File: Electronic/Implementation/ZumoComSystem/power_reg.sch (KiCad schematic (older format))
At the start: 5 parts, among them J1 AudioJack2_SwitchT, U1 LT1374CS8-5PBF, U2 TPS62056DGS

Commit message: electronic -> Schematic -> add hierarchical pins, modified Regulator page
           -> BOM & Clac: add new inductors
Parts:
- removed J1: AudioJack2_SwitchT, Button_Switch_THT:SW_E-Switch_EG1224_SPDT_Angled, symbol Connector:AudioJack2_SwitchT
- added C1, C?: >10u, symbol Device:C
- added C2: >22u, symbol Device:C
- added C? (x3): C, symbol Device:C
- added D?: D, symbol Device:D
- added M1: MPMOS, symbol pspice:MPMOS
- added SW1: MLL1200S, SW_MLL1200S, symbol MLL1200S:MLL1200S
- L2: value 6uH -> 22uH
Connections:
- net labels added: +3V3, +5V, GND, V_Bat
- wire segments 2 -> 72
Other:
- moved on the sheet: L1, L2, U1, U2

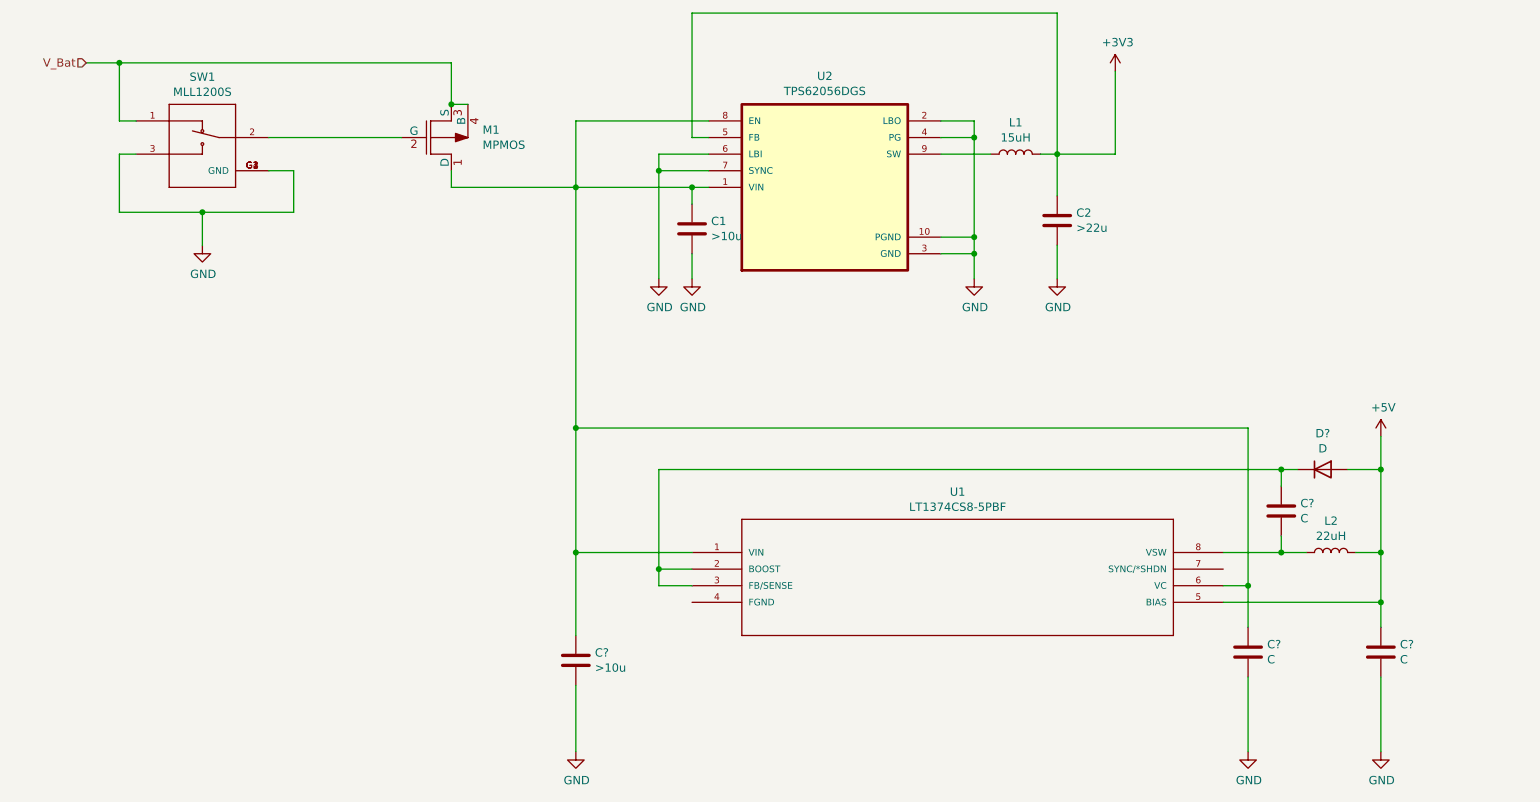
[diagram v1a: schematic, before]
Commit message: Electronic -> Schematic -> DC/DC -> add C, L with footprint, datasheet
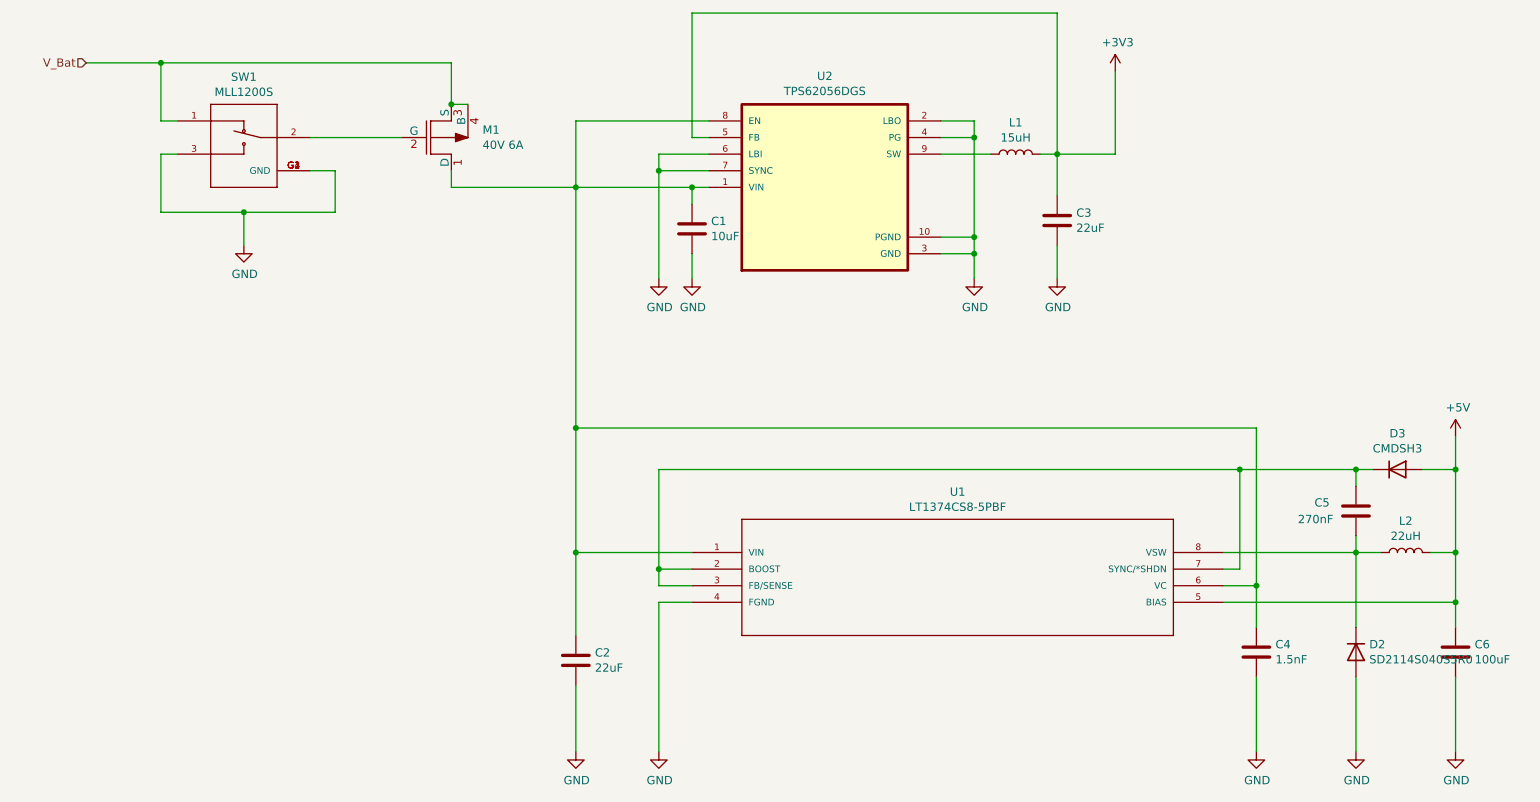
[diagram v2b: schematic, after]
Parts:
- removed C2: >22u, symbol Device:C
- added C3: 22uF, Capacitor_SMD:C_1206_3216Metric_Pad1.42x1.75mm_HandSolder, symbol Device:C
- added D2: SD2114S040S5R0, Diode_SMD:D_2114_3652Metric_Pad1.85x3.75mm_HandSolder, symbol Device:D
- C1: value >10u -> 10uF; footprint (none) -> Capacitor_SMD:C_0805_2012Metric_Pad1.15x1.40mm_HandSolder
- C2: renamed from C?; value >10u -> 22uF; footprint (none) -> Capacitor_SMD:C_1206_3216Metric_Pad1.42x1.75mm_HandSolder
- C4: renamed from C?; value C -> 1.5nF; footprint (none) -> Capacitor_SMD:C_0603_1608Metric_Pad1.05x0.95mm_HandSolder
- C5: renamed from C?; value C -> 270nF; footprint (none) -> Capacitor_SMD:C_0805_2012Metric_Pad1.15x1.40mm_HandSolder
- C6: renamed from C?; value C -> 100uF; footprint (none) -> Capacitor_SMD:C_1206_3216Metric_Pad1.42x1.75mm_HandSolder
- D3: renamed from D?; value D -> CMDSH3; footprint (none) -> Diode_SMD:D_SOD-323
- M1: value MPMOS -> 40V 6A; footprint (none) -> Package_TO_SOT_SMD:SOT-89-3_Handsoldering
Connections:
- net +3V3: now also C3.1
- net GND: now also U1.4 (FGND), C3.2, D2.2 (A)
- net at C5.1, D3.1 (K), U1.2 (BOOST)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: now also U1.7 (SYNC/*SHDN)
- net at C5.2, L2.1, U1.8 (VSW): now also D2.1 (K)
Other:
- moved on the sheet: C4, C5, C6, D3, L2, SW1

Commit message: Electronic: Schematic: ESP I/Os, IF_Pololu Pins, USB_max
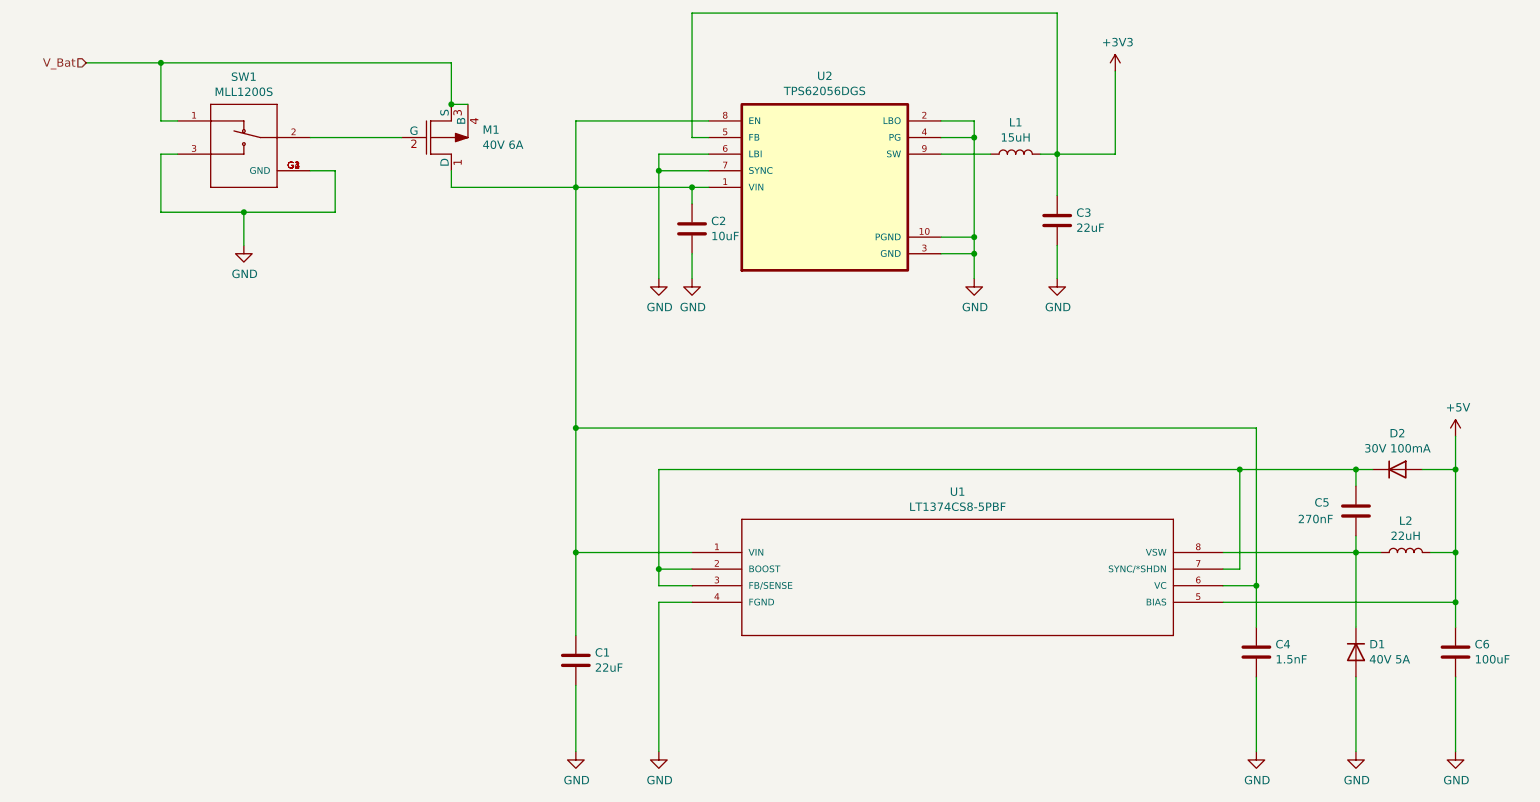
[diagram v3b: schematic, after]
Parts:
- D1: renamed from D2; value SD2114S040S5R0 -> 40V 5A
- D2: renamed from D3; value CMDSH3 -> 30V 100mA
- renumbered C2 to C1, C1 to C2
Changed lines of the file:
@@
 Sheet 2 7
 Title "Zumo Communication System"
-Date "2021-06-25"
+Date "2021-07-28"
 Rev "V1.0"
 Comp "NewTec GmbH"
@@
 V_Bat
 $Comp
-L power:+3V3 #PWR0101
+L power:+3V3 #PWR08
 U 1 1 60CC7A1E
 P 7200 1300
-F 0 "#PWR0101" H 7200 1150 50  0001 C CNN
+F 0 "#PWR08" H 7200 1150 50  0001 C CNN
 F 1 "+3V3" H 7215 1473 50  0000 C CNN
 F 2 "" H 7200 1300 50  0001 C CNN
@@
 $EndComp
 $Comp
-L power:+5V #PWR0102
+L power:+5V #PWR011
 U 1 1 60CC818D
 P 9250 3500
-F 0 "#PWR0102" H 9250 3350 50  0001 C CNN
+F 0 "#PWR011" H 9250 3350 50  0001 C CNN
 F 1 "+5V" H 9265 3673 50  0000 C CNN
 F 2 "" H 9250 3500 50  0001 C CNN
@@
 	4750 1600 3950 1600
 $Comp
-L power:GND #PWR0103
+L power:GND #PWR06
 U 1 1 60CDA80F
 P 6350 2550
-F 0 "#PWR0103" H 6350 2300 50  0001 C CNN
+F 0 "#PWR06" H 6350 2300 50  0001 C CNN
 F 1 "GND" H 6355 2377 50  0000 C CNN
 F 2 "" H 6350 2550 50  0001 C CNN
@@
 Connection ~ 6350 2300
 $Comp
-L power:GND #PWR0104
+L power:GND #PWR03
 U 1 1 60CDABA5
 P 4450 2550
-F 0 "#PWR0104" H 4450 2300 50  0001 C CNN
+F 0 "#PWR03" H 4450 2300 50  0001 C CNN
 F 1 "GND" H 4455 2377 50  0000 C CNN
 F 2 "" H 4450 2550 50  0001 C CNN
@@
 	6850 1800 6750 1800
 $Comp
-L Device:C C1
+L Device:C C2
 U 1 1 60CE065A
 P 4650 2250
-F 0 "C1" H 4765 2296 50  0000 L CNN
+F 0 "C2" H 4765 2296 50  0000 L CNN
 F 1 "10uF" H 4765 2205 50  0000 L CNN
 F 2 "Capacitor_SMD:C_0805_2012Metric_Pad1.15x1.40mm_HandSolder" H 4688 2100 50  0001 C CNN
@@
 	4650 2400 4650 2550
 $Comp
-L power:GND #PWR0105
+L power:GND #PWR05
 U 1 1 60CE2DC8
 P 4650 2550
-F 0 "#PWR0105" H 4650 2300 50  0001 C CNN
+F 0 "#PWR05" H 4650 2300 50  0001 C CNN
 F 1 "GND" H 4655 2377 50  0000 C CNN
 F 2 "" H 4650 2550 50  0001 C CNN
@@
 $EndComp
 $Comp
-L power:GND #PWR0106
+L power:GND #PWR07
 U 1 1 60CE2EFC
 P 6850 2550
-F 0 "#PWR0106" H 6850 2300 50  0001 C CNN
+F 0 "#PWR07" H 6850 2300 50  0001 C CNN
 F 1 "GND" H 6855 2377 50  0000 C CNN
 F 2 "" H 6850 2550 50  0001 C CNN
@@
 	3200 1900 3200 2000
 $Comp
-L power:GND #PWR0107
+L power:GND #PWR01
 U 1 1 60CF3E43
 P 1950 2350
-F 0 "#PWR0107" H 1950 2100 50  0001 C CNN
+F 0 "#PWR01" H 1950 2100 50  0001 C CNN
 F 1 "GND" H 1955 2177 50  0000 C CNN
 F 2 "" H 1950 2350 50  0001 C CNN
@@
 Wire Wire Line
 	1950 2150 2500 2150
-$Comp
-L pspice:MPMOS M1
-U 1 1 60D049A0
-P 3100 1700
-F 0 "M1" H 3388 1746 50  0000 L CNN
-F 1 "40V 6A" H 3388 1655 50  0000 L CNN
-F 2 "Package_TO_SOT_SMD:SOT-89-3_Handsoldering" H 3100 1700 50  0001 C CNN
-F 3 "https://my.centralsemi.com/datasheets/CXDM4060P.PDF" H 3100 1700 50  0001 C CNN
-	1    3100 1700
-	1    0    0    -1
-$EndComp
 Wire Wire Line
 	3300 1500 3200 1500
 Connection ~ 3200 1500
 $Comp
-L Device:C C2
+L Device:C C1
 U 1 1 60D11B75
 P 3950 4850
-F 0 "C2" H 4065 4896 50  0000 L CNN
+F 0 "C1" H 4065 4896 50  0000 L CNN
 F 1 "22uF" H 4065 4805 50  0000 L CNN
 F 2 "Capacitor_SMD:C_1206_3216Metric_Pad1.42x1.75mm_HandSolder" H 3988 4700 50  0001 C CNN
@@
 	4650 4300 4450 4300
 $Comp
-L power:GND #PWR01
+L power:GND #PWR02
 U 1 1 60D140B6
 P 3950 5400
-F 0 "#PWR01" H 3950 5150 50  0001 C CNN
+F 0 "#PWR02" H 3950 5150 50  0001 C CNN
 F 1 "GND" H 3955 5227 50  0000 C CNN
 F 2 "" H 3950 5400 50  0001 C CNN
@@
 	3950 5400 3950 5000
 $Comp
-L Device:D D3
+L Device:D D2
 U 1 1 60D196DD
 P 8900 3700
-F 0 "D3" H 8900 3917 50  0000 C CNN
-F 1 "CMDSH3 " H 8900 3826 50  0000 C CNN
+F 0 "D2" H 8900 3917 50  0000 C CNN
+F 1 "30V 100mA" H 8900 3826 50  0000 C CNN
 F 2 "Diode_SMD:D_SOD-323" H 8900 3700 50  0001 C CNN
 F 3 "https://my.centralsemi.com/datasheets/CMDSH-3.PDF" H 8900 3700 50  0001 C CNN
@@
 	8050 4650 8050 4400
 $Comp
-L power:GND #PWR03
+L power:GND #PWR09
 U 1 1 60D2AA9B
 P 8050 5400
-F 0 "#PWR03" H 8050 5150 50  0001 C CNN
+F 0 "#PWR09" H 8050 5150 50  0001 C CNN
 F 1 "GND" H 8055 5227 50  0000 C CNN
 F 2 "" H 8050 5400 50  0001 C CNN
@@
 $EndComp
 $Comp
-L power:GND #PWR05
+L power:GND #PWR012
 U 1 1 60D2B041
 P 9250 5400
-F 0 "#PWR05" H 9250 5150 50  0001 C CNN
+F 0 "#PWR012" H 9250 5150 50  0001 C CNN
 F 1 "GND" H 9255 5227 50  0000 C CNN
 F 2 "" H 9250 5400 50  0001 C CNN
@@
 	9250 3700 9250 3500
 $Comp
-L Device:D D2
+L Device:D D1
 U 1 1 60D62CCC
 P 8650 4800
-F 0 "D2" V 8604 4880 50  0000 L CNN
-F 1 "SD2114S040S5R0" V 8695 4880 50  0000 L CNN
+F 0 "D1" V 8604 4880 50  0000 L CNN
+F 1 "40V 5A" V 8695 4880 50  0000 L CNN
 F 2 "Diode_SMD:D_2114_3652Metric_Pad1.85x3.75mm_HandSolder" H 8650 4800 50  0001 C CNN
 F 3 "https://datasheets.avx.com/schottky.pdf" H 8650 4800 50  0001 C CNN
@@
 $EndComp
 $Comp
-L power:GND #PWR04
+L power:GND #PWR010
 U 1 1 60D630D3
 P 8650 5400
-F 0 "#PWR04" H 8650 5150 50  0001 C CNN
+F 0 "#PWR010" H 8650 5150 50  0001 C CNN
 F 1 "GND" H 8655 5227 50  0000 C CNN
 F 2 "" H 8650 5400 50  0001 C CNN
@@
 	4450 4500 4450 5400
 $Comp
-L power:GND #PWR02
+L power:GND #PWR04
 U 1 1 60D67CF9
 P 4450 5400
-F 0 "#PWR02" H 4450 5150 50  0001 C CNN
+F 0 "#PWR04" H 4450 5150 50  0001 C CNN
 F 1 "GND" H 4455 5227 50  0000 C CNN
 F 2 "" H 4450 5400 50  0001 C CNN
@@
 Wire Wire Line
 	1000 1250 1450 1250
+$Comp
+L pspice:MPMOS M1
+U 1 1 60D049A0
+P 3100 1700
+F 0 "M1" H 3388 1746 50  0000 L CNN
+F 1 "40V 6A" H 3388 1655 50  0000 L CNN
+F 2 "Package_TO_SOT_SMD:SOT-89-3_Handsoldering" H 3100 1700 50  0001 C CNN
+F 3 "https://my.centralsemi.com/datasheets/CXDM4060P.PDF" H 3100 1700 50  0001 C CNN
+	1    3100 1700
+	1    0    0    -1
+$EndComp
 $EndSCHEMATC

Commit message: Electronic: no charger, added Cp2102 instead of Ft232, first palcement
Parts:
- removed M1: 40V 6A, Package_TO_SOT_SMD:SOT-89-3_Handsoldering, symbol pspice:MPMOS
- added Q1: Q_PMOS_GDS, footprints:TSOT-23-6_HandSoldering, symbol Device:Q_PMOS_GDS
- added R1, R2: 100k, Resistor_SMD:R_0603_1608Metric_Pad1.05x0.95mm_HandSolder, symbol Device:R
- L1: footprint Inductor_SMD:L_Wuerth_HCI-1040 -> footprints:L_Wuerth_HCI-1040_3D
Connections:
- net GND: now also R2.1
- net V_Bat: now also Q1.3 (S)
- net at C1.1, C2.1, C4.1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: now also Q1.2 (D)
- net at SW1.2: now also R1.2
- new net: Q1.1 (G), R1.1, R2.2
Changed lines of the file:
@@
 Sheet 2 7
 Title "Zumo Communication System"
-Date "2021-08-20"
+Date "2022-03-08"
 Rev "V1.0"
 Comp "NewTec GmbH"
@@
 F 0 "L1" V 6790 1800 50  0000 C CNN
 F 1 "15uH" V 6699 1800 50  0000 C CNN
-F 2 "Inductor_SMD:L_Wuerth_HCI-1040" H 6600 1800 50  0001 C CNN
+F 2 "footprints:L_Wuerth_HCI-1040_3D" H 6600 1800 50  0001 C CNN
 F 3 "https://www.we-online.de/katalog/datasheet/74437368150.pdf" H 6600 1800 50  0001 C CNN
 	1    6600 1800
@@
 V_Bat
 $Comp
-L power:+3V3 #PWR08
+L power:+3V3 #PWR09
 U 1 1 60CC7A1E
 P 7200 1300
-F 0 "#PWR08" H 7200 1150 50  0001 C CNN
+F 0 "#PWR09" H 7200 1150 50  0001 C CNN
 F 1 "+3V3" H 7215 1473 50  0000 C CNN
 F 2 "" H 7200 1300 50  0001 C CNN
@@
 $EndComp
 $Comp
-L power:+5V #PWR011
+L power:+5V #PWR012
 U 1 1 60CC818D
 P 9250 3500
-F 0 "#PWR011" H 9250 3350 50  0001 C CNN
+F 0 "#PWR012" H 9250 3350 50  0001 C CNN
 F 1 "+5V" H 9265 3673 50  0000 C CNN
 F 2 "" H 9250 3500 50  0001 C CNN
@@
 	4750 1600 3950 1600
 $Comp
-L power:GND #PWR06
+L power:GND #PWR07
 U 1 1 60CDA80F
 P 6350 2550
-F 0 "#PWR06" H 6350 2300 50  0001 C CNN
+F 0 "#PWR07" H 6350 2300 50  0001 C CNN
 F 1 "GND" H 6355 2377 50  0000 C CNN
 F 2 "" H 6350 2550 50  0001 C CNN
@@
 Connection ~ 6350 2300
 $Comp
-L power:GND #PWR03
+L power:GND #PWR04
 U 1 1 60CDABA5
 P 4450 2550
-F 0 "#PWR03" H 4450 2300 50  0001 C CNN
+F 0 "#PWR04" H 4450 2300 50  0001 C CNN
 F 1 "GND" H 4455 2377 50  0000 C CNN
 F 2 "" H 4450 2550 50  0001 C CNN
@@
 	4650 2400 4650 2550
 $Comp
-L power:GND #PWR05
+L power:GND #PWR06
 U 1 1 60CE2DC8
 P 4650 2550
-F 0 "#PWR05" H 4650 2300 50  0001 C CNN
+F 0 "#PWR06" H 4650 2300 50  0001 C CNN
 F 1 "GND" H 4655 2377 50  0000 C CNN
 F 2 "" H 4650 2550 50  0001 C CNN
@@
 $EndComp
 $Comp
-L power:GND #PWR07
+L power:GND #PWR08
 U 1 1 60CE2EFC
 P 6850 2550
-F 0 "#PWR07" H 6850 2300 50  0001 C CNN
+F 0 "#PWR08" H 6850 2300 50  0001 C CNN
 F 1 "GND" H 6855 2377 50  0000 C CNN
 F 2 "" H 6850 2550 50  0001 C CNN
@@
 	7200 1800 7200 1300
 Wire Wire Line
-	3200 2000 3950 2000
-Wire Wire Line
-	3200 1250 3200 1500
-Wire Wire Line
-	3200 1900 3200 2000
+	3250 2000 3350 2000
 $Comp
 L power:GND #PWR01
@@
 Wire Wire Line
 	1950 2150 2500 2150
-Wire Wire Line
-	3300 1500 3200 1500
-Connection ~ 3200 1500
 $Comp
 L Device:C C1
@@
 	4650 4300 4450 4300
 $Comp
-L power:GND #PWR02
+L power:GND #PWR03
 U 1 1 60D140B6
 P 3950 5400
-F 0 "#PWR02" H 3950 5150 50  0001 C CNN
+F 0 "#PWR03" H 3950 5150 50  0001 C CNN
 F 1 "GND" H 3955 5227 50  0000 C CNN
 F 2 "" H 3950 5400 50  0001 C CNN
@@
 	8050 4650 8050 4400
 $Comp
-L power:GND #PWR09
+L power:GND #PWR010
 U 1 1 60D2AA9B
 P 8050 5400
-F 0 "#PWR09" H 8050 5150 50  0001 C CNN
+F 0 "#PWR010" H 8050 5150 50  0001 C CNN
 F 1 "GND" H 8055 5227 50  0000 C CNN
 F 2 "" H 8050 5400 50  0001 C CNN
@@
 $EndComp
 $Comp
-L power:GND #PWR012
+L power:GND #PWR013
 U 1 1 60D2B041
 P 9250 5400
-F 0 "#PWR012" H 9250 5150 50  0001 C CNN
+F 0 "#PWR013" H 9250 5150 50  0001 C CNN
 F 1 "GND" H 9255 5227 50  0000 C CNN
 F 2 "" H 9250 5400 50  0001 C CNN
@@
 $EndComp
 $Comp
-L power:GND #PWR010
+L power:GND #PWR011
 U 1 1 60D630D3
 P 8650 5400
-F 0 "#PWR010" H 8650 5150 50  0001 C CNN
+F 0 "#PWR011" H 8650 5150 50  0001 C CNN
 F 1 "GND" H 8655 5227 50  0000 C CNN
 F 2 "" H 8650 5400 50  0001 C CNN
@@
 	4450 4500 4450 5400
 $Comp
-L power:GND #PWR04
+L power:GND #PWR05
 U 1 1 60D67CF9
 P 4450 5400
-F 0 "#PWR04" H 4450 5150 50  0001 C CNN
+F 0 "#PWR05" H 4450 5150 50  0001 C CNN
 F 1 "GND" H 4455 5227 50  0000 C CNN
 F 2 "" H 4450 5400 50  0001 C CNN
@@
 Wire Wire Line
 	1450 1600 1450 1250
-Wire Wire Line
-	2350 1700 2900 1700
 Connection ~ 1450 1250
 Wire Wire Line
-	1450 1250 3200 1250
+	1450 1250 3250 1250
 Wire Wire Line
 	1000 1250 1450 1250
 $Comp
-L pspice:MPMOS M1
-U 1 1 60D049A0
-P 3100 1700
-F 0 "M1" H 3388 1746 50  0000 L CNN
-F 1 "40V 6A" H 3388 1655 50  0000 L CNN
-F 2 "Package_TO_SOT_SMD:SOT-89-3_Handsoldering" H 3100 1700 50  0001 C CNN
-F 3 "https://my.centralsemi.com/datasheets/CXDM4060P.PDF" H 3100 1700 50  0001 C CNN
-	1    3100 1700
-	1    0    0    -1
+L Device:R R1
+U 1 1 62459142
+P 2600 1700
+F 0 "R1" V 2393 1700 50  0000 C CNN
+F 1 "100k" V 2484 1700 50  0000 C CNN
+F 2 "Resistor_SMD:R_0603_1608Metric_Pad1.05x0.95mm_HandSolder" V 2530 1700 50  0001 C CNN
+F 3 "~" H 2600 1700 50  0001 C CNN
+	1    2600 1700
+	0    1    1    0
+$EndComp
+$Comp
+L Device:R R2
+U 1 1 6245A145
+P 2850 2000
+F 0 "R2" H 2780 1954 50  0000 R CNN
+F 1 "100k" H 2780 2045 50  0000 R CNN
+F 2 "Resistor_SMD:R_0603_1608Metric_Pad1.05x0.95mm_HandSolder" V 2780 2000 50  0001 C CNN
+F 3 "~" H 2850 2000 50  0001 C CNN
+	1    2850 2000
+	-1   0    0    1
+$EndComp
+Wire Wire Line
+	2350 1700 2450 1700
+Wire Wire Line
+	2750 1700 2850 1700
+Wire Wire Line
+	2850 2350 2850 2150
+Wire Wire Line
+	2850 1850 2850 1700
+Connection ~ 2850 1700
+Wire Wire Line
+	2850 1700 3550 1700
+$Comp
+L power:GND #PWR02
+U 1 1 62464A3F
+P 2850 2350
+F 0 "#PWR02" H 2850 2100 50  0001 C CNN
+F 1 "GND" H 2855 2177 50  0000 C CNN
+F 2 "" H 2850 2350 50  0001 C CNN
+F 3 "" H 2850 2350 50  0001 C CNN
+	1    2850 2350
+	1    0    0    -1
+$EndComp
+Wire Wire Line
+	3750 2000 3950 2000
+Wire Wire Line
+	3250 1250 3250 2000
+$Comp
+L Device:Q_PMOS_GDS Q1
+U 1 1 624703BF
+P 3550 1900
+F 0 "Q1" V 3799 1900 50  0000 C CNN
+F 1 "Q_PMOS_GDS" V 3890 1900 50  0000 C CNN
+F 2 "footprints:TSOT-23-6_HandSoldering" H 3750 2000 50  0001 C CNN
+F 3 "https://www.diodes.com/assets/Datasheets/DMP6023LE.pdf" H 3550 1900 50  0001 C CNN
+	1    3550 1900
+	0    1    1    0
 $EndComp
 $EndSCHEMATC

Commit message: Electronic: PCB routed
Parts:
- Q1: value Q_PMOS_GDS -> PMOS-RQ5C060BCTCL; footprint footprints:TSOT-23-6_HandSoldering -> footprints:SOT95P280X100-3N
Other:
- note added: "Imax = 200 mA"
- note added: "U_Bat_max = 8.4 V\nI_Bat_max = 4,2 A"
- note added: "\nImax = 3 A"
- moved on the sheet: Q1
